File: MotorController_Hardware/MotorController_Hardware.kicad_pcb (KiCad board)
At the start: 2 copper layers, 124.5 x 150.9 mm, 246 parts, among them Q12 FQP30N06L, Q13 FQP30N06L, Q14 FQP30N06L, Q15 FQP30N06L, Q16 FQP30N06L, Q17 FQP30N06L, Q4 FQP30N06L, Q5 FQP30N06L, Q6 FQP30N06L, Q7 FQP30N06L, Q8 FQP30N06L, Q9 FQP30N06L, U1 DRV8301, U2 NUP4201MR6, U3 LAUNCHXL_F28069M_Launchpad, U4 MAX_3232, U5 DRV8301, U6 NUP4201MR6

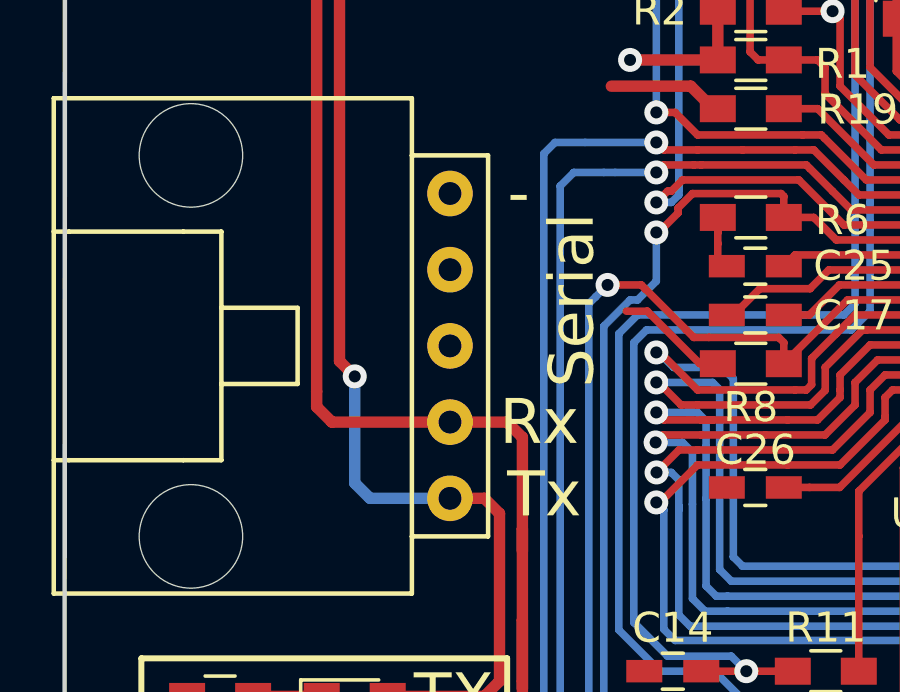
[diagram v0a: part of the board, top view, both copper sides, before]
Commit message: Schematic finished and footprints assigned
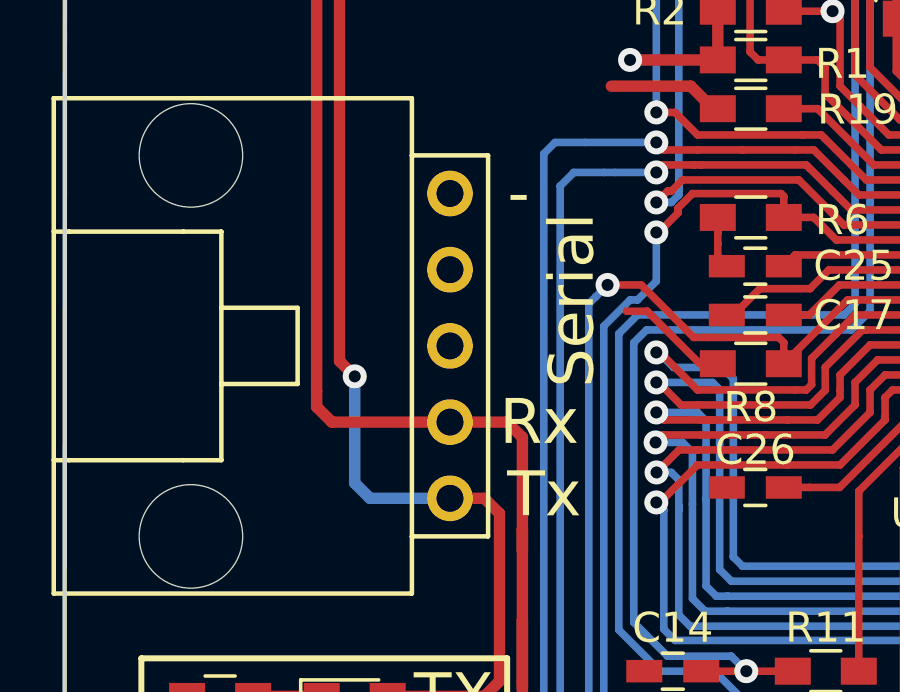
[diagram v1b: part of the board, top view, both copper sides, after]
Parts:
- U1, U5: value DRV8301 -> DCA56_6P35X3P61

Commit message: high level layout
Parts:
- removed C37, C38, C39: 220u, Capacitors_THT:CP_Radial_D10.0mm_P5.00mm
- removed C45: 470u, Capacitors_THT:CP_Radial_D12.5mm_P5.00mm
- removed C47: 0.1u, Capacitors_SMD:C_1206_HandSoldering
- removed C48: 0.01u, Capacitors_SMD:C_1206_HandSoldering
- removed C49, C50, C53, C56, C58, C61, C62, C63, C75, C76, C77: 0.1u, Capacitors_SMD:C_0603_HandSoldering
- removed C51, C55: 4.7u, Capacitors_SMD:C_0805_HandSoldering
- removed C52, C68, C69: 1u, Capacitors_SMD:C_0603_HandSoldering
- removed C54: 47u, Capacitor_THT:CP_Radial_D6.3mm_P2.50mm
- removed C57, C59: 2200p, Capacitors_SMD:C_0603_HandSoldering
- removed C60: .022u, Capacitors_SMD:C_0603_HandSoldering
- removed C64: 0.015u, Capacitors_SMD:C_0603_HandSoldering
- removed C65: 120p, Capacitors_SMD:C_0603_HandSoldering
- removed C66: 6800p, Capacitors_SMD:C_0603_HandSoldering
- removed C67: 2.2u, Capacitors_SMD:C_0603_HandSoldering
- removed C70, C71: 1000p, Capacitors_SMD:C_0603_HandSoldering
- removed C72, C73, C74: 2.2u, Capacitors_SMD:C_1206_HandSoldering
- removed Conn10: SH_B_M2_PP, MRDT_Connectors:Anderson_1_Horizontal
- removed Conn11: SH_C_M2_PP, MRDT_Connectors:Anderson_1_Horizontal
- removed Conn8: AndersonPP, MRDT_Connectors:Anderson_2_Horizontal_Stacked
- removed Conn9: SH_A_M2_PP, MRDT_Connectors:Anderson_1_Horizontal
- removed D13, D14, D22, D23, D24, D25, D26, D27, D28, D29, D30, D31, D32, D33, D34, D37, D5, D6: LED, LEDs:LED_0603_HandSoldering
- removed D15: D_Schottky, Diodes_SMD:D_SOD-123
- removed D16, D17, D18, D19, D20, D21: 3.3V, Diodes_SMD:D_SOD-123
- removed G***: LOGO, MRDT_Silkscreens:Andrew_Van_Horn_Sig_15mm
- removed G***: LOGO, MRDT_Silkscreens:Shaun_McManus_Sig_15mm
- removed G***: LOGO, MRDT_Silkscreens:MRDT_Logo_20mm
- removed GHA_M1: tp, Wire_Pads:SolderWirePad_single_1mmDrill
- removed GHA_M2, GHB_M1, GHB_M2, GHC_M1, GHC_M2, GLA_M1, GLA_M2, GLB_M1, GLB_M2, GLC_M1, GLC_M2, PVDD_M1, PVDD_M2, SHA_M1, SHA_M2, SHB_M1, SHB_M2, SHC_M1, SHC_M2: TEST, Wire_Pads:SolderWirePad_single_1mmDrill
- removed L2: 33u, MRDT_Passives:DR74_330_R
- removed Q12, Q13, Q14, Q15, Q16, Q17: FQP30N06L, MRDT_Actives:TO-220-3_Horizontal_Reversed_NoHole
- removed R17, R21, R36, R37, R64, R65, R66, R67, R68, R69, R70, R71, R72, R73, R74, R75: 500, Resistors_SMD:R_0603_HandSoldering
- removed R38, R39, R40, R43: 10k, Resistors_SMD:R_0603_HandSoldering
- removed R41, R44: 1k, Resistors_SMD:R_0603_HandSoldering
- removed R42: 31.6k, Resistors_SMD:R_0603_HandSoldering
- removed R45, R46: 56, Resistors_SMD:R_0603_HandSoldering
- removed R47: 205k, Resistors_SMD:R_0603_HandSoldering
- removed R48: 150k, Resistors_SMD:R_0603_HandSoldering
- removed R49: 16.2k, Resistors_SMD:R_0603_HandSoldering
- removed R50, R51, R52, R53, R54, R55: 10, Resistors_SMD:R_0603_HandSoldering
- removed R56, R57: .001, Resistors_SMD:R_1206_HandSoldering
- removed R58, R60, R62, R79: 46.4k, Resistors_SMD:R_0603_HandSoldering
- removed R59, R61, R63, R80: 4.99k, Resistors_SMD:R_0603_HandSoldering
- removed R78: 3.3, Resistors_SMD:R_1206_HandSoldering
- removed R81: 1.5K, Resistors_SMD:R_0603_HandSoldering
- removed the REF** at (54.6, 18.3)
- removed the REF** at (58.6, -34.4)
- removed the REF** at (167.0, -34.4)
- removed the REF** at (170.9, 18.3)
- removed U3: LAUNCHXL_F28069M_Launchpad, MRDT_Shields:LAUNCHXL_F28069M_FULL_SMD_BOTTOM
- removed U5: DCA56_6P35X3P61, MRDT_ICs:DRV8301
- removed U6: NUP4201MR6, MRDT_ICs:NUP4201MR6
- added C11: 470u, Capacitor_THT:CP_Radial_D12.5mm_P5.00mm, F.Cu at (177.8, 66.0)
- added Q1: Q_PMOS_DGS, Package_TO_SOT_SMD:SOT-23_Handsoldering, F.Cu at (240.5, 115.5)
- added Q2: Q_PMOS_DGS, Package_TO_SOT_SMD:SOT-23_Handsoldering, F.Cu at (225.8, 133.8)
- added REF**: LAUNCHXL_F28027M, MRDT_Shields:F28027M_THT_TOP, F.Cu at (127.0, 127.0)
- +3V3: footprint Wire_Pads:SolderWirePad_single_1mmDrill -> Package_TO_SOT_SMD:SOT-23_Handsoldering
- C1, C10, C12, C13, C14, C17, C18, C19, C20, C21, C22, C23, C24, C25, C26, C27, C28, C29, C3, C33, C34, C35, C4, C40, C41, C42, C43, C44: footprint Capacitors_SMD:C_0603_HandSoldering -> Capacitor_SMD:C_0603_1608Metric_Pad1.05x0.95mm_HandSolder
- C15, C16, C30, C31, C32: footprint Capacitors_SMD:C_1206_HandSoldering -> Capacitor_SMD:C_0603_1608Metric_Pad1.05x0.95mm_HandSolder
- C2, C8: footprint Capacitors_SMD:C_0805_HandSoldering -> Capacitor_SMD:C_0603_1608Metric_Pad1.05x0.95mm_HandSolder
- C36: value 220u -> C_Small; footprint Capacitors_THT:CP_Radial_D10.0mm_P5.00mm -> Capacitor_SMD:C_0603_1608Metric_Pad1.05x0.95mm_HandSolder
- C5, C7: value 220u -> 470u; footprint Capacitors_THT:CP_Radial_D10.0mm_P5.00mm -> Capacitor_THT:CP_Radial_D12.5mm_P5.00mm
- C9: footprint Capacitors_THT:CP_Radial_D12.5mm_P5.00mm -> Capacitor_THT:CP_Radial_D12.5mm_P5.00mm
- D1: footprint Diodes_SMD:D_SOD-123 -> Diode_SMD:D_SOD-123
- D10, D11, D12, D7, D8, D9: value 3.3V -> 15V; footprint Diodes_SMD:D_SOD-123 -> Diode_SMD:D_SOD-123
- D2, D3, D4: footprint LEDs:LED_0603_HandSoldering -> Inductor_SMD:L_0603_1608Metric_Pad1.05x0.95mm_HandSolder
- Q4, Q5, Q6, Q7, Q8, Q9: moved to F.Cu
- R1, R11, R12, R13, R15, R16, R18, R19, R2, R20, R22, R23, R24, R25, R26, R27, R3, R30, R31, R32, R33, R34, R35, R4, R5, R6, R8, R9: footprint Resistors_SMD:R_0603_HandSoldering -> Resistor_SMD:R_0603_1608Metric_Pad1.05x0.95mm_HandSolder
- R10: value 1.5K -> 500; footprint Resistors_SMD:R_0603_HandSoldering -> Resistor_SMD:R_0603_1608Metric_Pad1.05x0.95mm_HandSolder
- R14, R28, R29: footprint Resistors_SMD:R_1206_HandSoldering -> Resistor_SMD:R_1206_3216Metric_Pad1.42x1.75mm_HandSolder
- R7: value 500 -> R; footprint Resistors_SMD:R_0603_HandSoldering -> Resistor_SMD:R_0603_1608Metric_Pad1.05x0.95mm_HandSolder
- U1: value DCA56_6P35X3P61 -> DRV8301
- moved C31 232.4 mm to (281.3, 102.9), turned to 0 degrees
- moved C36 231.9 mm to (276.9, 105.9), turned to 0 degrees
- moved C28 228.8 mm to (279.9, 97.9), turned to 0 degrees
- moved C44 228.2 mm to (272.6, 110.9), turned to 0 degrees
- moved C41 226.3 mm to (272.6, 105.9), turned to 0 degrees
- moved C40 221.3 mm to (268.2, 108.4), turned to 0 degrees
- moved C42 221.2 mm to (272.6, 108.4)
- moved C29 220.5 mm to (284.2, 97.9), turned to 0 degrees
- moved R13 218.4 mm to (268.2, 110.9)
- moved D2 216.4 mm to (268.2, 113.4), turned to 0 degrees
- moved C32 214.0 mm to (272.6, 103.4), turned to 0 degrees
- moved R9 213.5 mm to (256.8, 127.0)
- moved C30 210.7 mm to (281.3, 100.4), turned to 0 degrees
- moved C43 205.0 mm to (245.4, 119.0), turned to 0 degrees
- moved C27 200.8 mm to (281.3, 95.4), turned to 0 degrees
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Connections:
- net ASENSE_M1 renamed ASENSE
- net BSENSE_M1 renamed BSENSE
- net CSENSE_M1 renamed CSENSE
- net DC_CAL_M1 renamed DC_CAL
- net EN_GATE_M1 renamed EN_GATE
- net GH_A_M1 renamed GH_A
- net GH_B_M1 renamed GH_B
- net GH_C_M1 renamed GH_C
- net GL_A_M1 renamed GL_A
- net GL_B_M1 renamed GL_B
- net GL_C_M1 renamed GL_C
- net MGH_B_M1 renamed /MGH_B_M1
- net MGH_C_M1 renamed /MGH_C_M1
- net MGL_A_M1 renamed /MGL_A_M1
- net MGL_B_M1 renamed /MGL_B_M1
- net MGL_C_M1 renamed /MGL_C_M1
- net NFAULT_M1 renamed NFAULT
- net NOCTW_M1 renamed NOCTW
- net PVDDSENSE_M1 renamed PVDDSENSE
- net PWRGD_M1 renamed PWRGD
- net SH_A_M1 renamed SH_A
- net SH_B_M1 renamed SH_B
- net SH_C_M1 renamed SH_C
- net SL_A_M1 renamed SL_A
- net SL_B_M1 renamed SL_B
- net SO1_M1 renamed SO1
- net SO2_M1 renamed SO2
- C1 pad 1: Net-(C1-Pad1) -> +3V3
- C10 pad 1: PVDD_M1 -> PVDD
- C13 pad 1: +3V3 -> Net-(C13-Pad1)
- C15 pad 1: PVDD_M1 -> PVDD
- C16 pad 1: PVDD_M1 -> PVDD
- C2 pad 1: PVDD_M1 -> PVDD
- C3 pad 1: Net-(C1-Pad1) -> +3V3
- C30 pad 1: PVDD_M1 -> PVDD
- C31 pad 1: PVDD_M1 -> PVDD
- C32 pad 1: PVDD_M1 -> PVDD
- C36 pad 1: PVDD_M1 -> Net-(C36-Pad1)
- C4 pad 1: PVDD_M1 -> PVDD
- C5 pad 1: PVDD_M2 -> PVDD
- C6 pad 1: Net-(C1-Pad1) -> +3V3
- C7 pad 1: PVDD_M2 -> PVDD
- C8 pad 1: PVDD_M1 -> PVDD
- C9 pad 1: PVDD_M1 -> PVDD
- Conn1 pad 1: SL_TX -> Net-(Conn1-Pad1)
- Conn1 pad 2: SL_RX -> Net-(Conn1-Pad2)
- Conn1 pad 3: (no net) -> GND
- Conn1 pad 4: (no net) -> SL_RX
- Conn1 pad 5: GND -> SL_TX
- Conn3 pad 4: PVDD_M1 -> PVDD
- D1 pad 1: +3V3 -> Net-(C13-Pad1)
- D2 pad 2: MGH_A_M1 -> VCC
- D3 pad 2: PVDD_M1 -> Net-(D3-Pad2)
- D4 pad 2: +3V3 -> Net-(D4-Pad2)
- D7 pad 1: MGH_A_M1 -> /MGH_A_M1
- L1 pad 1: Net-(C1-Pad1) -> +3V3
- L1 pad 2: +3V3 -> Net-(C13-Pad1)
- Q4 pad 1: MGH_A_M1 -> /MGH_A_M1
- Q4 pad 2: PVDD_M1 -> PVDD
- Q6 pad 2: PVDD_M1 -> PVDD
- Q8 pad 2: PVDD_M1 -> PVDD
- R10 pad 1: GND -> Net-(D3-Pad1)
- R10 pad 2: Net-(D3-Pad1) -> GND
- R13 pad 1: GND -> Net-(D4-Pad1)
- R13 pad 2: Net-(D6-Pad1) -> GND
- R15 pad 1: PVDD_M1 -> PVDD
- R22 pad 1: MGH_A_M1 -> /MGH_A_M1
- R7 pad 1: GND -> Net-(Conn1-Pad1)
- R7 pad 2: Net-(D4-Pad1) -> Net-(C36-Pad1)
- R9 pad 1: GND -> Net-(D2-Pad1)
- R9 pad 2: Net-(D5-Pad1) -> GND
- U1 pad 10: SDO_M1 -> SDO
- U1 pad 11: SCLK_M1 -> SCLK
- U1 pad 17: INH_A_M1 -> INH_A
- U1 pad 18: INL_A_M1 -> INL_A
- U1 pad 19: INH_B_M1 -> INH_B
- U1 pad 20: INL_B_M1 -> INL_B
- U1 pad 21: INH_C_M1 -> INH_C
- U1 pad 22: INL_C_M1 -> INL_C
- U1 pad 29: PVDD_M1 -> PVDD
- U1 pad 50: +3V3 -> Net-(C13-Pad1)
- U1 pad 51: +3V3 -> Net-(U1-Pad51)
- U1 pad 53: PVDD_M1 -> PVDD
- U1 pad 54: PVDD_M1 -> PVDD
- U1 pad 55: (no net) -> Net-(U1-Pad55)
- U1 pad 8: NSCS_M1 -> NSCS
- U1 pad 9: SDI_M1 -> SDI
- U4 pad 10: UART_TX -> Net-(U4-Pad10)
- U4 pad 11: (no net) -> UART_TX
- U4 pad 12: (no net) -> UART_RX
- U4 pad 13: (no net) -> SL_RX
- U4 pad 14: (no net) -> SL_TX
- U4 pad 7: SL_TX -> Net-(U4-Pad7)
- U4 pad 8: SL_RX -> Net-(U4-Pad8)
- U4 pad 9: UART_RX -> Net-(U4-Pad9)
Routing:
- net GND: track 224.2 -> 0.00 mm, vias 21 -> 0
- net SL_A: track 185.2 -> 0.00 mm, vias 2 -> 0
- net SH_A_M2: track 182.3 -> 0.00 mm, vias 3 -> 0
- net UART_TX: track 181.6 -> 0.00 mm, vias 3 -> 0
- net SL_A_M2: track 181.3 -> 0.00 mm, vias 2 -> 0
- net PVDD_M2: track 161.0 -> 0.00 mm, vias 2 -> 0
- net SL_B: track 157.7 -> 0.00 mm, vias 2 -> 0
- net MGH_A_M2: track 155.1 -> 0.00 mm, vias 1 -> 0
- net UART_RX: track 151.9 -> 0.00 mm, vias 3 -> 0
- net SH_B_M2: track 151.7 -> 0.00 mm, vias 3 -> 0
- net MGL_A_M2: track 146.1 -> 0.00 mm, vias 1 -> 0
- net SL_B_M2: track 144.2 -> 0.00 mm, vias 2 -> 0
- net SH_A: track 140.0 -> 0.00 mm, vias 3 -> 0
- net /MGL_A_M1: track 135.2 -> 0.00 mm, vias 1 -> 0
- net PVDD_M1: track 130.3 -> 0.00 mm, vias 4 -> 0
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- removed copper zone on F.Cu, net (none)
- removed copper zone on B.Cu, net +3V3
- removed copper zone on F.Cu, net GND
- removed copper zone on B.Cu, net PVDD_M1
- removed copper zone on B.Cu, net PVDD_M2
- removed copper zone on F.Cu, net SH_A
- removed copper zone on F.Cu, net SH_A_M2
- removed copper zone on F.Cu, net SH_B
- removed copper zone on F.Cu, net SH_B_M2
- removed copper zone on F.Cu, net SH_C
- removed copper zone on F.Cu, net SH_C_M2
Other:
- board outline removed
- copper layers 2 -> 4
- board text removed: "+"
- board text removed: "+3V3"
- board text removed: "-"
- board text removed: "4-40"
- board text removed: "A1"
- board text removed: "A2"
- board text removed: "B1"
- board text removed: "B2"
- board text removed: "Brushless Motor Controller, Rev 1 Mars Rover Design Team Missouri S&T, 2019 Schematic: Shaun McManus Layout: Andrew Van Horn Original Design by Cameron Nichols (2017)"
- board text removed: "C1"
- board text removed: "C2"
- board text removed: "DRV 8301"
- board text removed: "FAULT_M1"
- board text removed: "FAULT_M2"
- board text removed: "GHA_M1"
- board text removed: "GHA_M2"
- board text removed: "GHB_M1"
- board text removed: "GHB_M2"
- board text removed: "GHC_M1"
- board text removed: "GHC_M2"
- board text removed: "GLA_M1"
- board text removed: "GLA_M2"
- board text removed: "GLB_M1"
- board text removed: "GLB_M2"
- board text removed: "GLC_M1"
- board text removed: "GLC_M2"
- board text removed: "OCTW_M1"
- board text removed: "OCTW_M2"
- board text removed: "PVDD_M1"
- board text removed: "PVDD_M2"
- board text removed: "Power"
- board text removed: "R O V E S O H A R D"
- board text removed: "RX"
- board text removed: "Rx"
- board text removed: "Serial"
- board text removed: "TODAY TOMORROW FOREVER"
- board text removed: "TX"
- board text removed: "Tx"

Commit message: PCB layout: In progress
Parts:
- C28, Q4, Q5, Q6, Q7, Q8, Q9, R28: moved to B.Cu
- moved C15 237.0 mm to (39.1, 60.5)
- moved C36 234.8 mm to (42.4, 95.2)
- moved R16 216.1 mm to (37.1, 67.1)
- moved C16 209.8 mm to (46.9, 68.1)
- moved R7 209.4 mm to (42.1, 90.2)
- moved R15 207.5 mm to (38.0, 78.5)
- moved R14 206.7 mm to (48.3, 56.9)
- moved C21 205.9 mm to (46.7, 63.5)
- moved U2 202.9 mm to (42.4, 114.3)
- moved C32 202.3 mm to (80.3, 166.1)
- moved C35 191.6 mm to (97.5, 168.1)
- moved C29 187.8 mm to (133.1, 209.3)
- moved C31 186.3 mm to (137.7, 221.5)
- moved D12 180.9 mm to (109.2, 170.7)
- moved R26 180.3 mm to (87.9, 167.1)
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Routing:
- added copper zone on B.Cu, net GND
- added copper zone on F.Cu, net GND
- added copper zone on In1.Cu, net GND
- added copper zone on In2.Cu, net PVDD
- added copper zone on B.Cu, net SL_A
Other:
- board outline added: 106.8 x 80 mm

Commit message: Work done on PCB layout
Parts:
- removed REF**: LAUNCHXL_F28027M, MRDT_Shields:F28027M_THT_TOP
- added U3: F28027M, MRDT_Shields:F28027M_THT_TOP, F.Cu at (127.0, 127.0)
- C29, D10, D11, D12, D7, D8, D9, R22, R23, R24, R25, R26, R27, R29, U2: moved to B.Cu
- C36: value C_Small -> .015 uF
- moved C31 155.2 mm to (137.3, 66.3), turned to 90 degrees
- moved R29 152.9 mm to (159.1, 72.8)
- moved R27 151.2 mm to (192.8, 73.0), turned to 270 degrees
- moved R25 149.4 mm to (156.8, 80.5), turned to 270 degrees
- moved D9 149.1 mm to (138.5, 77.2)
- moved R5 144.5 mm to (123.3, 97.3), turned to 180 degrees
- moved R24 143.0 mm to (134.1, 77.0)
- moved R1 142.8 mm to (118.5, 101.3)
- moved R2 140.5 mm to (123.3, 99.8)
- moved R4 138.5 mm to (118.5, 96.0)
- moved C29 136.5 mm to (159.0, 75.3)
- moved D10 136.5 mm to (152.5, 77.1)
- moved C14 133.8 mm to (132.1, 89.8), turned to 180 degrees
- moved R3 132.2 mm to (118.5, 98.6)
- moved C32 132.1 mm to (166.6, 66.2), turned to 90 degrees
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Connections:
- net Net-(C36-Pad1) renamed PWM_IN
- D2 pad 2: VCC -> +3V3
- Q1 pad 3: VCC -> +3V3
- Q2 pad 3: VCC -> +3V3
- U2 pad 2: +3V3 -> GND
- U2 pad 5: GND -> +3V3
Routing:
- net /MGL_C_M1: track 0.00 -> 14.2 mm
- net /MGL_B_M1: track 0.00 -> 11.7 mm
- net /MGH_B_M1: track 0.00 -> 9.14 mm
- net /MGH_C_M1: track 0.00 -> 6.63 mm
- net /MGL_A_M1: track 0.00 -> 6.34 mm
- net Net-(C40-Pad2): track 0.00 -> 6.17 mm
- net Net-(R4-Pad2): track 0.00 -> 5.79 mm
- net GND: track 0.00 -> 5.49 mm, vias 0 -> 3
- net /MGH_A_M1: track 0.00 -> 5.48 mm
- net SH_B: track 0.00 -> 4.49 mm
- net Net-(C41-Pad1): track 0.00 -> 3.89 mm
- net SH_A: track 0.00 -> 3.57 mm
- net Net-(C16-Pad2): track 0.00 -> 3.33 mm
- net Net-(C44-Pad2): track 0.00 -> 3.12 mm
- net Net-(C43-Pad2): track 0.00 -> 3.11 mm
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- added copper zone on F.Cu, net PVDD
- added copper zone on B.Cu, net SL_B
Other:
- board size 106.8 x 80 mm -> 112.9 x 80 mm

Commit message: Update MotorController_Hardware.kicad_pcb
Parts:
- moved C20 100.0 mm to (150.6, 114.7), turned to 90 degrees
- moved C19 99.4 mm to (153.2, 110.2), turned to 270 degrees
- moved C18 0.76 mm to (155.6, 105.9)
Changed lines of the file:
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@@
   )
   (module Capacitor_SMD:C_0603_1608Metric_Pad1.05x0.95mm_HandSolder (layer F.Cu)
-    (at 156.337 105.918 270)
+    (at 155.575 105.918 270)
     (descr "Capacitor SMD 0603 (1608 Metric), square (rectangular) end terminal, IPC_7351 nominal with elongated pad for handsoldering. (Body size source: http://www.tortai-tech.com/upload/download/2011102023233369053.pdf), generated with kicad-footprint-generator")
     (tags "capacitor handsolder")
@@
   )
   (module Capacitor_SMD:C_0603_1608Metric_Pad1.05x0.95mm_HandSolder (layer F.Cu)
-    (at 246.888 143.256)
+    (at 153.162 110.25 270)
     (descr "Capacitor SMD 0603 (1608 Metric), square (rectangular) end terminal, IPC_7351 nominal with elongated pad for handsoldering. (Body size source: http://www.tortai-tech.com/upload/download/2011102023233369053.pdf), generated with kicad-footprint-generator")
     (tags "capacitor handsolder")
     (attr smd)
-    (fp_text reference C19 (at 0 -1.43) (layer F.SilkS)
+    (fp_text reference C19 (at 0 -1.43 90) (layer F.SilkS)
       (effects (font (size 1 1) (thickness 0.15)))
     )
-    (fp_text value 0.1u (at 0 1.43) (layer F.Fab)
+    (fp_text value 0.1u (at 0 1.43 270) (layer F.Fab)
       (effects (font (size 1 1) (thickness 0.15)))
     )
@@
     (fp_line (start 1.65 -0.73) (end 1.65 0.73) (layer F.CrtYd) (width 0.05))
     (fp_line (start 1.65 0.73) (end -1.65 0.73) (layer F.CrtYd) (width 0.05))
-    (fp_text user %R (at 0 0) (layer F.Fab)
+    (fp_text user %R (at 0 0 90) (layer F.Fab)
       (effects (font (size 0.4 0.4) (thickness 0.06)))
     )
-    (pad 1 smd roundrect (at -0.875 0) (size 1.05 0.95) (layers F.Cu F.Paste F.Mask) (roundrect_rratio 0.25)
+    (pad 1 smd roundrect (at -0.875 0 270) (size 1.05 0.95) (layers F.Cu F.Paste F.Mask) (roundrect_rratio 0.25)
       (net 6 "Net-(C19-Pad1)"))
-    (pad 2 smd roundrect (at 0.875 0) (size 1.05 0.95) (layers F.Cu F.Paste F.Mask) (roundrect_rratio 0.25)
+    (pad 2 smd roundrect (at 0.875 0 270) (size 1.05 0.95) (layers F.Cu F.Paste F.Mask) (roundrect_rratio 0.25)
       (net 39 SH_B))
     (model ${KISYS3DMOD}/Capacitor_SMD.3dshapes/C_0603_1608Metric.wrl
@@
   )
   (module Capacitor_SMD:C_0603_1608Metric_Pad1.05x0.95mm_HandSolder (layer F.Cu)
-    (at 248.045 137.16)
+    (at 150.622 114.667 90)
     (descr "Capacitor SMD 0603 (1608 Metric), square (rectangular) end terminal, IPC_7351 nominal with elongated pad for handsoldering. (Body size source: http://www.tortai-tech.com/upload/download/2011102023233369053.pdf), generated with kicad-footprint-generator")
     (tags "capacitor handsolder")
     (attr smd)
-    (fp_text reference C20 (at 0 -1.43) (layer F.SilkS)
+    (fp_text reference C20 (at 0 1.524 90) (layer F.SilkS)
       (effects (font (size 1 1) (thickness 0.15)))
     )
-    (fp_text value 0.1u (at 0 1.43) (layer F.Fab)
+    (fp_text value 0.1u (at 0 1.43 90) (layer F.Fab)
       (effects (font (size 1 1) (thickness 0.15)))
     )
-    (fp_text user %R (at 0 0) (layer F.Fab)
+    (fp_text user %R (at 0 0 90) (layer F.Fab)
       (effects (font (size 0.4 0.4) (thickness 0.06)))
     )
@@
     (fp_line (start -0.8 -0.4) (end 0.8 -0.4) (layer F.Fab) (width 0.1))
     (fp_line (start -0.8 0.4) (end -0.8 -0.4) (layer F.Fab) (width 0.1))
-    (pad 2 smd roundrect (at 0.875 0) (size 1.05 0.95) (layers F.Cu F.Paste F.Mask) (roundrect_rratio 0.25)
+    (pad 2 smd roundrect (at 0.875 0 90) (size 1.05 0.95) (layers F.Cu F.Paste F.Mask) (roundrect_rratio 0.25)
       (net 40 SH_C))
-    (pad 1 smd roundrect (at -0.875 0) (size 1.05 0.95) (layers F.Cu F.Paste F.Mask) (roundrect_rratio 0.25)
+    (pad 1 smd roundrect (at -0.875 0 90) (size 1.05 0.95) (layers F.Cu F.Paste F.Mask) (roundrect_rratio 0.25)
       (net 7 "Net-(C20-Pad1)"))
     (model ${KISYS3DMOD}/Capacitor_SMD.3dshapes/C_0603_1608Metric.wrl

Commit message: Finished PCB layout
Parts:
- +3V3: footprint Package_TO_SOT_SMD:SOT-23_Handsoldering -> MRDT_Drill_Holes:Via_.6mm
- moved C27 158.9 mm to (125.2, 120.5)
- moved R8 139.9 mm to (115.8, 112.1), turned to 270 degrees
- moved C26 129.9 mm to (123.0, 116.1)
- moved R6 128.2 mm to (121.2, 104.5), turned to 180 degrees
- moved C25 119.9 mm to (120.9, 109.5)
- moved C13 113.2 mm to (146.3, 104.5), turned to 90 degrees
- moved R19 108.6 mm to (125.1, 104.4), turned to 180 degrees
- moved C10 107.2 mm to (141.8, 123.2)
- moved C17 104.1 mm to (124.9, 109.3)
- moved C8 94.6 mm to (141.8, 120.4)
- moved C3 93.4 mm to (191.3, 109.7), turned to 180 degrees
- moved +3V3 88.3 mm to (160.3, 80.5)
- moved R7 86.9 mm to (119.5, 129.5)
- moved C36 83.8 mm to (120.4, 125.9), turned to 90 degrees
- moved C1 66.2 mm to (191.3, 107.1), turned to 180 degrees
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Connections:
- U1 pad 51: Net-(U1-Pad51) -> Net-(C13-Pad1)
- U3 pad +3V3: (no net) -> +3V3
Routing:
- net +3V3: track 2.92 -> 265.1 mm, vias 0 -> 9
- net SL_TX: track 0.00 -> 144.3 mm, vias 0 -> 2
- net SL_RX: track 0.00 -> 143.2 mm, vias 0 -> 1
- net SH_C: track 0.00 -> 115.5 mm, vias 0 -> 2
- net SH_A: track 3.57 -> 115.9 mm, vias 0 -> 2
- net NFAULT: track 0.00 -> 109.1 mm, vias 0 -> 3
- net NOCTW: track 0.00 -> 101.2 mm, vias 0 -> 3
- net GH_A: track 0.00 -> 94.3 mm, vias 0 -> 1
- net SL_A: track 0.00 -> 94.3 mm, vias 0 -> 2
- net GL_C: track 0.00 -> 90.4 mm, vias 0 -> 3
- net SH_B: track 4.49 -> 89.4 mm, vias 0 -> 3
- net GL_A: track 0.00 -> 80.6 mm, vias 0 -> 1
- net NSCS: track 0.00 -> 79.6 mm, vias 0 -> 1
- net GH_B: track 0.00 -> 69.1 mm, vias 0 -> 1
- net SDI: track 0.00 -> 67.2 mm, vias 0 -> 1
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- added copper zone on In1.Cu, net SH_A
- added copper zone on In1.Cu, net SH_B
- added copper zone on In1.Cu, net SH_C

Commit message: Silkscreens added
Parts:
- added G***: LOGO, MRDT_Silkscreens:z_sig_Austin_Christman_22mmx8.3mm, F.Cu at (179.5, 129.5)
- added G***: LOGO, MRDT_Silkscreens:z_sig_Brian_Dahlman_Sig_20.1mmX7.5mm, F.Cu at (159.8, 129.2)
- added G***: LOGO, MRDT_Silkscreens:2_Dahlbot_2.0, F.Cu at (189.9, 120.5)
- added GHA_M1: tp, MRDT_Drill_Holes:Via_.6mm, F.Cu at (99.2, 82.9)
- added GHB_M1: TEST, MRDT_Drill_Holes:Via_.6mm, F.Cu at (130.7, 77.9)
- added GHC_M1: TEST, MRDT_Drill_Holes:Via_.6mm, F.Cu at (161.2, 77.6)
- added GLA_M1: TEST, MRDT_Drill_Holes:Via_.6mm, F.Cu at (114.7, 77.9)
- added GLB_M1: TEST, MRDT_Drill_Holes:Via_.6mm, F.Cu at (146.2, 77.6)
- added GLC_M1: TEST, MRDT_Drill_Holes:Via_.6mm, F.Cu at (178.3, 77.6)
- added PVDD_M1: TEST, MRDT_Drill_Holes:Via_.6mm, F.Cu at (92.7, 118.4)
- added SHA_M1: TEST, MRDT_Drill_Holes:Via_.6mm, F.Cu at (111.1, 77.9)
- added SHB_M1: TEST, MRDT_Drill_Holes:Via_.6mm, F.Cu at (143.1, 77.6)
- added SHC_M1: TEST, MRDT_Drill_Holes:Via_.6mm, F.Cu at (173.0, 77.6)
- moved C9 2.71 mm to (93.3, 75.9)
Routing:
- net /MGH_A_M1: track 5.48 -> 13.4 mm
- net /MGL_C_M1: track 14.2 -> 19.3 mm
- net SH_C: track 115.5 -> 119.5 mm
- net /MGL_B_M1: track 10.8 -> 14.3 mm
- net /MGH_C_M1: track 6.63 -> 10.1 mm
- net SH_A: track 115.9 -> 119.3 mm
- net /MGH_B_M1: track 9.14 -> 12.4 mm
- net SH_B: track 89.4 -> 92.6 mm
- net /MGL_A_M1: track 6.34 -> 9.39 mm
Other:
- board text added: "+3V3 Power"
- board text added: "+3V3 TEST"
- board text added: "GND"
- board text added: "MGH_A TEST"
- board text added: "MGH_B TEST"
- board text added: "MGH_C TEST"
- board text added: "MGL_A TEST"
- board text added: "MGL_B TEST"
- board text added: "MGL_C TEST"
- board text added: "Motor Controller Rev1 Mars Rover Design Team Missouri S&T, 2020 Cameron Nichols"
- board text added: "NC"
- board text added: "PVDD TEST"
- board text added: "PWM_IN"
- board text added: "SH_A TEST"
- board text added: "SH_B TEST"
- board text added: "SH_C TEST"
- board text added: "SL_RX"
- board text added: "SL_TX"

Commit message: WORKING ON ORDERING
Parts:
- removed G***: LOGO, MRDT_Silkscreens:z_sig_Austin_Christman_22mmx8.3mm
- removed G***: LOGO, MRDT_Silkscreens:z_sig_Brian_Dahlman_Sig_20.1mmX7.5mm
- removed G***: LOGO, MRDT_Silkscreens:2_Dahlbot_2.0
- added D5: LED, Inductor_SMD:L_0603_1608Metric_Pad1.05x0.95mm_HandSolder, F.Cu at (93.5, 122.9)
- added R17: 0, Resistor_SMD:R_0603_1608Metric_Pad1.05x0.95mm_HandSolder, B.Cu at (128.4, 78.6)
- added R21: 0, Resistor_SMD:R_0603_1608Metric_Pad1.05x0.95mm_HandSolder, B.Cu at (159.9, 78.1)
- added R36: 1000, Resistor_SMD:R_0603_1608Metric_Pad1.05x0.95mm_HandSolder, F.Cu at (97.5, 122.8)
- D1: value D_Shottky -> D_Zener; footprint Diode_SMD:D_SOD-123 -> Diode_SMD:D_0603_1608Metric_Pad1.05x0.95mm_HandSolder
- R7: value R -> 100
- R9: value 500 -> 510
- moved R25 5.41 mm to (151.7, 79.1)
- moved D1 1.76 mm to (150.2, 100.7)
- moved C28 0.19 mm to (127.5, 75.2)
- moved U3 0.06 mm to (126.9, 127.0)
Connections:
- U1 pad 30: GND -> SP2
- U1 pad 32: GND -> SP1
- U3 pad GND: GND -> Net-(U3-PadGND)
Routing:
- net SP1: track 0.00 -> 75.9 mm, vias 0 -> 1
- net SP2: track 0.00 -> 53.7 mm, vias 0 -> 1
- net GND: track 10.5 -> 21.0 mm, vias 3 -> 67
- net /MGL_B_M1: track 14.3 -> 10.1 mm
- net GL_B: track 49.6 -> 52.0 mm
- net Net-(D5-Pad1): track 0.00 -> 2.34 mm
- net SH_C: track 119.5 -> 117.7 mm
- net SL_B: track 64.0 -> 65.6 mm
- net GL_C: track 90.4 -> 89.0 mm
- net GH_C: track 52.9 -> 52.1 mm
- net PVDD: track 57.6 -> 58.2 mm
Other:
- outline, holes or cut-outs redrawn
- board text added: "Motor Controller Rev1 Mars Rover Design Team Missouri S&T, 2020 Cameron Nichols Austin Christman, Brian Dahlman"
- board text removed: "Motor Controller Rev1 Mars Rover Design Team Missouri S&T, 2020 Cameron Nichols"
